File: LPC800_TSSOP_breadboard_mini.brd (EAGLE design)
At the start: 31.1 x 15.9 mm, 16 parts, among them Q1 12MHz

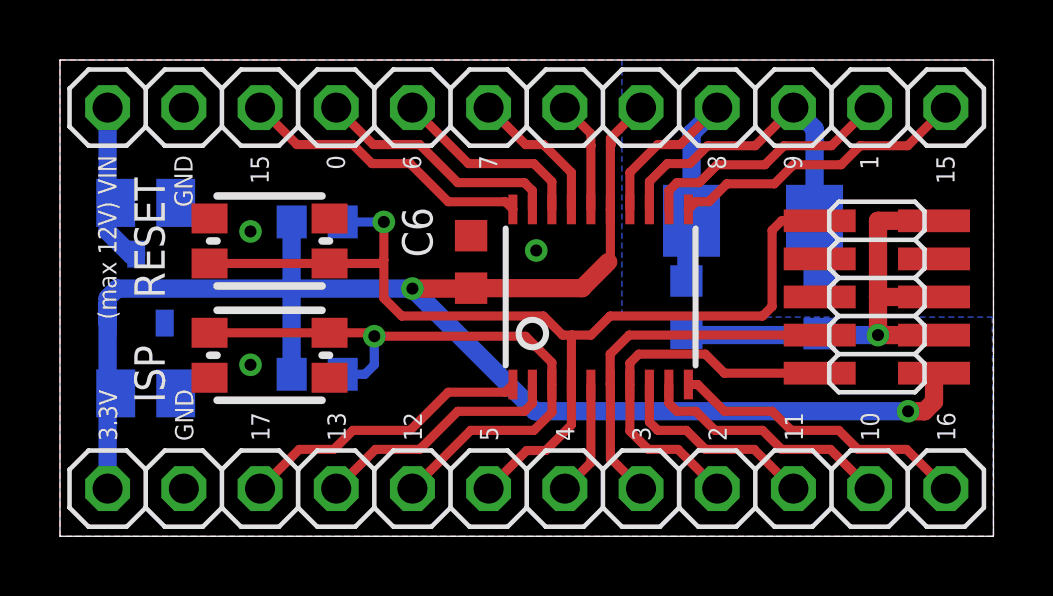
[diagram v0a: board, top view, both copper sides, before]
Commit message: * finished LPC800 mini board * fixed pin 1 for JTAG connection - TODO: Printout inspection and checks for the button layout
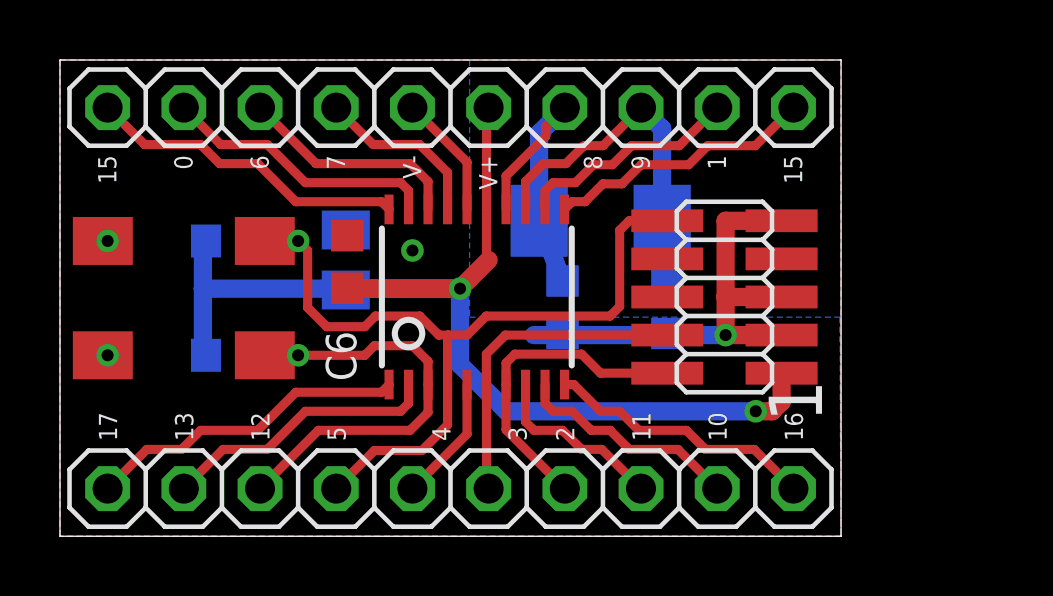
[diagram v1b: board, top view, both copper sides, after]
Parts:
- removed C5: 1u, bart_rcl:C0805K
- removed JP4, JP5: (no value), SquantorConnectors:1X12_NORMAL_OCT
- removed U$3: RESET, SquantorButtons:KMR2
- removed U$4: ISP, SquantorButtons:KMR2
- added JP1, JP2: (no value), SquantorConnectors:1X10_NORMAL_OCT
- added U$1: TACT_2PINDTSM3, SquantorButtons:DTSM3
- C6: value (none) -> 100n
- U$2: value TS9011 -> TACT_2PINDTSM3; device bart_ic:SOT23-3 -> SquantorButtons:DTSM3
- moved C4 8.01 mm to (9.53, 9.21), turned to 90 degrees
- moved C3 5.08 mm to (20.2, 7.63)
- moved JP3 5.08 mm to (22.1, 7.98)
- moved Q1 5.08 mm to (18.0, 10.5)
- moved C6 4.13 mm to (9.58, 9.14)
- moved LOGO2 4.13 mm to (14.5, 3.91)
- moved LPC812 4.13 mm to (13.9, 7.98)
- moved C2 4.13 mm to (16.8, 7.63)
- moved R1 2.93 mm to (5.71, 6.03)
- moved R2 2.93 mm to (5.71, 9.84)
- moved U$2 2.73 mm to (4.13, 6.03), flipped to the top, turned to 180 degrees
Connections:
- removed net VCCIO: C5.1, JP4.12, U$2.3
- net PIO0_0: now also JP2.9; no longer JP4.9
- net PIO0_1: now also JP2.2; no longer JP4.2
- net PIO0_10: now also JP1.9; no longer JP5.11
- net PIO0_11: now also JP1.8; no longer JP5.10
- net PIO0_12: now also JP1.3, U$2.P$1; no longer JP5.5, U$4.1, U$4.2
- net PIO0_13: now also JP1.2; no longer JP5.4
- net PIO0_14: now also JP2.10; no longer JP4.10
- net PIO0_15: now also JP2.1; no longer JP4.1
- net PIO0_16: now also JP1.10; no longer JP5.12
- net PIO0_17: now also JP1.1; no longer JP5.3
- net PIO0_2: now also JP1.7; no longer JP5.9
- net PIO0_3: now also JP1.6; no longer JP5.8
- net PIO0_4: now also JP1.5; no longer JP5.7
- net PIO0_5: now also JP1.4, U$1.P$1; no longer JP5.6, U$3.1, U$3.2
- net PIO0_6: now also JP2.8; no longer JP4.8
- net PIO0_7: now also JP2.7; no longer JP4.7
- net PIO0_8: now also JP2.4; no longer JP4.4
- net PIO0_9: now also JP2.3; no longer JP4.3
- net VDD: now also JP2.5; no longer JP4.5, JP5.1, U$2.2
- net VSS: now also JP2.6, U$1.P$2, U$2.P$2; no longer C5.2, JP4.11, JP4.6, JP5.2, U$2.1, U$3.3, U$3.4, U$4.3, U$4.4
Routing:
- net VDD: track 56.1 -> 38.4 mm
- net PIO0_5: track 34.9 -> 28.2 mm
- net PIO0_12: track 21.3 -> 15.5 mm
- net VCCIO: track 5.68 -> 0.00 mm
- net PIO0_2: track 12.7 -> 10.8 mm
- net PIO0_3: track 12.2 -> 10.8 mm
- net PIO0_1: track 8.46 -> 7.51 mm
- net PIO0_10: track 8.50 -> 7.54 mm
- net PIO0_7: track 4.89 -> 5.84 mm
- net PIO0_6: track 6.60 -> 7.55 mm
- net PIO0_17: track 9.87 -> 10.8 mm
- net PIO0_14: track 9.84 -> 10.8 mm
- net PIO0_13: track 8.34 -> 9.30 mm
- net PIO0_0: track 8.31 -> 9.26 mm
- net PIO0_15: track 9.99 -> 9.04 mm
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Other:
- board size 31.1 x 15.9 mm -> 26 x 15.9 mm
- board text added: "V+"
- board text added: "V-"
- board text removed: "(max 12V) VIN"
- board text removed: "3.3V"
- board text removed: "GND"

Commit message: * updated boards with cheaper buttons, better layout and indexed JTAG header
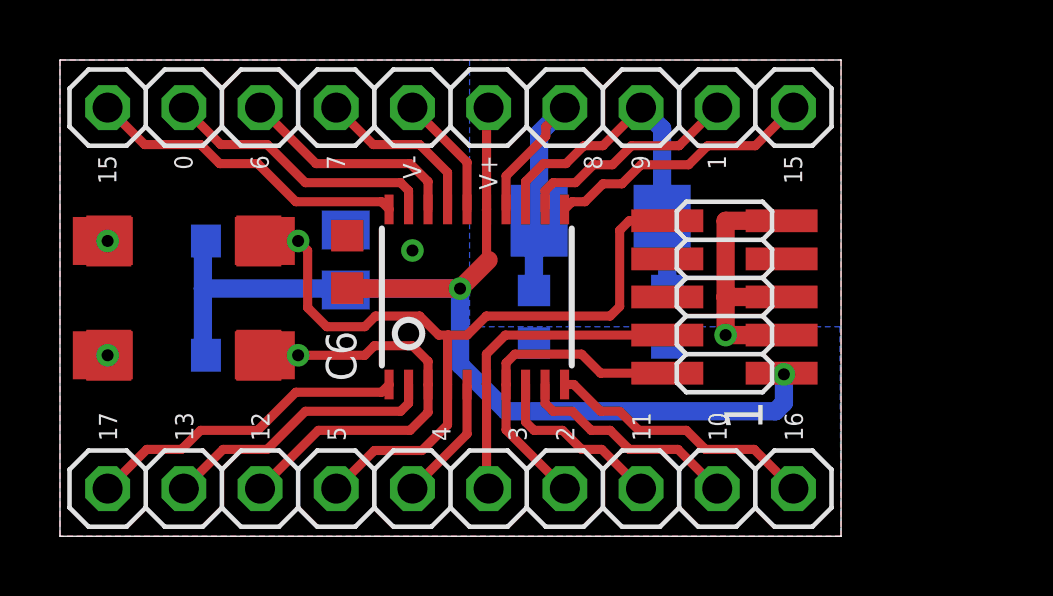
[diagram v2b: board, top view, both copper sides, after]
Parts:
- added U$3, U$4: TACT_2PIN, SquantorButtons:TD-85XU
- JP3: device bart_connectors:2X05_1.27_SMD -> SquantorConnectors:2X05_1.27_SMD
- moved C2 1.00 mm to (15.8, 7.32)
- moved C3 0.32 mm to (20.2, 7.32)
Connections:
- net PIO0_12: now also U$4.P$1
- net PIO0_5: now also U$3.P$1
- net VSS: now also U$3.P$2, U$4.P$2
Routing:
- net VSS: track 19.9 -> 13.6 mm
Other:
- board text added: "V2014.10.08"
- board text removed: "V2014.05.29"
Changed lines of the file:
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@@
 <?xml version="1.0" encoding="utf-8"?>
 <!DOCTYPE eagle SYSTEM "eagle.dtd">
-<eagle version="7.1.0">
+<eagle version="6.5.0">
 <drawing>
 <settings>
@@
 <layers>
 <layer number="1" name="Top" color="4" fill="1" visible="yes" active="yes"/>
-<layer number="16" name="Bottom" color="1" fill="1" visible="no" active="yes"/>
+<layer number="16" name="Bottom" color="1" fill="1" visible="yes" active="yes"/>
 <layer number="17" name="Pads" color="2" fill="1" visible="yes" active="yes"/>
 <layer number="18" name="Vias" color="2" fill="1" visible="yes" active="yes"/>
-<layer number="19" name="Unrouted" color="6" fill="1" visible="no" active="yes"/>
+<layer number="19" name="Unrouted" color="6" fill="1" visible="yes" active="yes"/>
 <layer number="20" name="Dimension" color="15" fill="1" visible="yes" active="yes"/>
 <layer number="21" name="tPlace" color="7" fill="1" visible="yes" active="yes"/>
-<layer number="22" name="bPlace" color="7" fill="1" visible="no" active="yes"/>
+<layer number="22" name="bPlace" color="7" fill="1" visible="yes" active="yes"/>
 <layer number="23" name="tOrigins" color="15" fill="1" visible="yes" active="yes"/>
-<layer number="24" name="bOrigins" color="15" fill="1" visible="no" active="yes"/>
+<layer number="24" name="bOrigins" color="15" fill="1" visible="yes" active="yes"/>
 <layer number="25" name="tNames" color="7" fill="1" visible="yes" active="yes"/>
-<layer number="26" name="bNames" color="7" fill="1" visible="no" active="yes"/>
+<layer number="26" name="bNames" color="7" fill="1" visible="yes" active="yes"/>
 <layer number="27" name="tValues" color="7" fill="1" visible="yes" active="yes"/>
-<layer number="28" name="bValues" color="7" fill="1" visible="no" active="yes"/>
+<layer number="28" name="bValues" color="7" fill="1" visible="yes" active="yes"/>
 <layer number="29" name="tStop" color="7" fill="3" visible="no" active="yes"/>
 <layer number="30" name="bStop" color="7" fill="6" visible="no" active="yes"/>
@@
 <wire x1="0" y1="15.875" x2="0" y2="0" width="0" layer="20"/>
 <wire x1="0" y1="0" x2="26.035" y2="0" width="0" layer="20"/>
-<text x="24.13" y="3.4925" size="1.016" layer="22" rot="MR90">V2014.05.29</text>
+<text x="24.13" y="3.4925" size="1.016" layer="22" rot="MR90">V2014.10.08</text>
 <text x="1.905" y="3.175" size="0.6096" layer="25" rot="R90">17</text>
 <text x="4.445" y="3.175" size="0.6096" layer="25" rot="R90">13</text>
@@
 <text x="11.43" y="12.7" size="0.6096" layer="25" rot="R270">V-</text>
 <text x="13.97" y="12.7" size="0.6096" layer="25" rot="R270">V+</text>
-<text x="25.4" y="3.81" size="1.778" layer="25" rot="R90">1</text>
 </plain>
 <attributes>
@@
 <pass name="Default">
 <param name="RoutingGrid" value="50mil"/>
-<param name="AutoGrid" value="1"/>
-<param name="Efforts" value="0"/>
-<param name="TopRouterVariant" value="1"/>
 <param name="tpViaShape" value="round"/>
 <param name="PrefDir.1" value="|"/>
@@
 <attribute name="VALUE" x="22.5425" y="8.255" size="1.016" layer="28" rot="MR90"/>
 </element>
-<element name="C2" library="SquantorRCL" package="C0603K" value="22p" x="16.7513" y="7.6327" smashed="yes" rot="MR270">
-<attribute name="NAME" x="14.6939" y="6.858" size="1.016" layer="26" rot="MR90"/>
-</element>
-<element name="C3" library="SquantorRCL" package="C0603K" value="22p" x="20.2438" y="7.6327" smashed="yes" rot="MR270">
-<attribute name="NAME" x="18.1864" y="6.858" size="1.016" layer="26" rot="MR90"/>
+<element name="C2" library="SquantorRCL" package="C0603K" value="22p" x="15.7988" y="7.3152" smashed="yes" rot="MR270">
+<attribute name="NAME" x="13.7414" y="6.5405" size="1.016" layer="26" rot="MR90"/>
+</element>
+<element name="C3" library="SquantorRCL" package="C0603K" value="22p" x="20.2438" y="7.3152" smashed="yes" rot="MR270">
+<attribute name="NAME" x="18.1864" y="6.5405" size="1.016" layer="26" rot="MR90"/>
 </element>
 <element name="LPC812" library="LPC800" package="TSSOP20" value="LPC812M101JDH20" x="13.8938" y="7.9756" smashed="yes"/>
-<element name="JP3" library="bart_connectors" package="2X05_1.27_SMD" value="JTAG" x="22.1488" y="7.9756" smashed="yes" rot="R90">
+<element name="JP3" library="SquantorConnectors" package="2X05_1.27_SMD" value="JTAG" x="22.1488" y="7.9756" smashed="yes" rot="R90">
 <attribute name="VALUE" x="18.6182" y="6.7437" size="1.016" layer="27" rot="R90"/>
 </element>
@@
 <element name="U$1" library="SquantorButtons" package="DTSM3" value="TACT_2PINDTSM3" x="4.1275" y="9.8425" smashed="yes" rot="R180"/>
 <element name="U$2" library="SquantorButtons" package="DTSM3" value="TACT_2PINDTSM3" x="4.1275" y="6.0325" smashed="yes" rot="R180"/>
+<element name="U$3" library="SquantorButtons" package="TD-85XU" value="TACT_2PIN" x="4.1275" y="9.8425" smashed="yes" rot="R180"/>
+<element name="U$4" library="SquantorButtons" package="TD-85XU" value="TACT_2PIN" x="4.1275" y="6.0325" smashed="yes" rot="R180"/>
 </elements>
 <signals>
@@
 <wire x1="15.5188" y1="11.8231" x2="16.1163" y2="12.4206" width="0.3048" layer="1"/>
 <wire x1="16.1163" y1="12.4206" x2="16.8656" y2="12.4206" width="0.3048" layer="1"/>
-<wire x1="20.2438" y1="8.5077" x2="20.2438" y2="10.9781" width="0.6096" layer="16"/>
+<wire x1="20.2438" y1="8.1902" x2="20.2438" y2="10.9781" width="0.6096" layer="16"/>
 <wire x1="20.2438" y1="10.9781" x2="20.0713" y2="10.5156" width="0.6096" layer="16"/>
 <wire x1="16.8656" y1="12.4206" x2="17.4625" y2="13.0175" width="0.3048" layer="1"/>
@@
 <contactref element="Q1" pad="1"/>
 <contactref element="C2" pad="1"/>
-<wire x1="16.7513" y1="8.5077" x2="15.7988" y2="10.9781" width="0.6096" layer="16"/>
+<wire x1="15.7988" y1="8.1902" x2="15.7988" y2="10.9781" width="0.6096" layer="16"/>
 <wire x1="15.7988" y1="10.9781" x2="15.9713" y2="10.5156" width="0.6096" layer="16"/>
 <wire x1="15.9713" y1="10.5156" x2="15.9713" y2="13.4313" width="0.6096" layer="16"/>
@@
 <via x="22.1869" y="6.7056" extent="1-16" drill="0.4" shape="octagon"/>
 <wire x1="22.1869" y1="6.7056" x2="24.0538" y2="6.7056" width="0.6096" layer="1"/>
-<wire x1="22.1869" y1="6.7056" x2="15.7988" y2="6.7056" width="0.6096" layer="16"/>
 <polygon width="0.254" layer="1" isolate="0.3048">
 <vertex x="0" y="15.875"/>
@@
 <vertex x="0" y="15.875"/>
 <vertex x="13.6525" y="15.875"/>
-<vertex x="13.6525" y="7.3025"/>
-<vertex x="25.9969" y="7.3025"/>
+<vertex x="13.6525" y="6.985"/>
+<vertex x="25.9969" y="6.985"/>
 <vertex x="26.035" y="0"/>
 <vertex x="0" y="0"/>
@@
 <wire x1="13.5688" y1="10.8934" x2="13.5688" y2="12.4662" width="0.3048" layer="1"/>
 <wire x1="13.5688" y1="12.4662" x2="11.7475" y2="14.2875" width="0.3048" layer="1"/>
+<contactref element="U$4" pad="P$2"/>
+<contactref element="U$3" pad="P$2"/>
 </signal>
 <signal name="VDD">
@@
 <contactref element="R2" pad="1"/>
 <wire x1="14.2113" y1="10.8859" x2="14.2188" y2="10.8934" width="0.3048" layer="1"/>
-<wire x1="24.0538" y1="5.4356" x2="24.0538" y2="4.4831" width="0.6096" layer="1"/>
-<via x="23.1902" y="4.1656" extent="1-16" drill="0.4" shape="octagon"/>
 <contactref element="C6" pad="1"/>
-<wire x1="24.0538" y1="4.4831" x2="23.7363" y2="4.1656" width="0.6096" layer="1"/>
-<wire x1="23.7363" y1="4.1656" x2="23.1902" y2="4.1656" width="0.6096" layer="1"/>
 <contactref element="JP2" pad="5"/>
 <contactref element="JP2" pad="5"/>
-<wire x1="23.1902" y1="4.1656" x2="14.8844" y2="4.1656" width="0.6096" layer="16"/>
+<wire x1="23.8506" y1="4.1656" x2="14.8844" y2="4.1656" width="0.6096" layer="16"/>
 <wire x1="14.8844" y1="4.1656" x2="13.335" y2="5.715" width="0.6096" layer="16"/>
 <wire x1="13.335" y1="5.715" x2="13.335" y2="8.255" width="0.6096" layer="16"/>
@@
 <wire x1="10.146" y1="8.269" x2="10.16" y2="8.255" width="0.6096" layer="1"/>
 <wire x1="10.16" y1="8.255" x2="13.335" y2="8.255" width="0.6096" layer="1"/>
+<wire x1="23.8506" y1="4.1656" x2="24.13" y2="4.445" width="0.6096" layer="16"/>
+<wire x1="24.13" y1="4.445" x2="24.13" y2="5.3975" width="0.6096" layer="16"/>
+<via x="24.13" y="5.3975" extent="1-16" drill="0.4" shape="octagon"/>
+<wire x1="24.13" y1="5.3975" x2="24.0919" y2="5.3975" width="0.6096" layer="1"/>
+<wire x1="24.0919" y1="5.3975" x2="24.0538" y2="5.4356" width="0.6096" layer="1"/>
 </signal>
 <signal name="PIO0_0">
@@
 <wire x1="7.9375" y1="9.8425" x2="8.255" y2="9.525" width="0.3048" layer="1"/>
 <wire x1="6.8275" y1="9.8425" x2="7.9375" y2="9.8425" width="0.3048" layer="1"/>
+<contactref element="U$3" pad="P$1"/>
+<wire x1="6.6275" y1="9.8425" x2="6.8275" y2="9.8425" width="0.4064" layer="1"/>
 </signal>
 <signal name="PIO0_6">
@@
 <wire x1="6.565" y1="6.0325" x2="7.9375" y2="6.0325" width="0.3048" layer="16"/>
 <via x="7.9375" y="6.0325" extent="1-16" drill="0.4" shape="octagon"/>
+<contactref element="U$4" pad="P$1"/>
+<wire x1="6.6275" y1="6.0325" x2="6.8275" y2="6.0325" width="0.4064" layer="1"/>
 </signal>
 <signal name="PIO0_11">

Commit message: * small changes preparing for commit to OSH park
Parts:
- moved C2 0.32 mm to (15.8, 7.00)
- moved C3 0.32 mm to (20.2, 7.00)
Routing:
- net VSS: track 13.6 -> 8.56 mm
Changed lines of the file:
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@@
 <?xml version="1.0" encoding="utf-8"?>
 <!DOCTYPE eagle SYSTEM "eagle.dtd">
-<eagle version="6.5.0">
+<eagle version="7.1.0">
 <drawing>
 <settings>
@@
 <layer number="20" name="Dimension" color="15" fill="1" visible="yes" active="yes"/>
 <layer number="21" name="tPlace" color="7" fill="1" visible="yes" active="yes"/>
-<layer number="22" name="bPlace" color="7" fill="1" visible="yes" active="yes"/>
+<layer number="22" name="bPlace" color="7" fill="1" visible="no" active="yes"/>
 <layer number="23" name="tOrigins" color="15" fill="1" visible="yes" active="yes"/>
-<layer number="24" name="bOrigins" color="15" fill="1" visible="yes" active="yes"/>
+<layer number="24" name="bOrigins" color="15" fill="1" visible="no" active="yes"/>
 <layer number="25" name="tNames" color="7" fill="1" visible="yes" active="yes"/>
-<layer number="26" name="bNames" color="7" fill="1" visible="yes" active="yes"/>
+<layer number="26" name="bNames" color="7" fill="1" visible="no" active="yes"/>
 <layer number="27" name="tValues" color="7" fill="1" visible="yes" active="yes"/>
-<layer number="28" name="bValues" color="7" fill="1" visible="yes" active="yes"/>
+<layer number="28" name="bValues" color="7" fill="1" visible="no" active="yes"/>
 <layer number="29" name="tStop" color="7" fill="3" visible="no" active="yes"/>
 <layer number="30" name="bStop" color="7" fill="6" visible="no" active="yes"/>
@@
 <wire x1="0" y1="15.875" x2="0" y2="0" width="0" layer="20"/>
 <wire x1="0" y1="0" x2="26.035" y2="0" width="0" layer="20"/>
-<text x="24.13" y="3.4925" size="1.016" layer="22" rot="MR90">V2014.10.08</text>
+<text x="23.1775" y="3.4925" size="1.016" layer="22" rot="MR0">V2014.10.08</text>
 <text x="1.905" y="3.175" size="0.6096" layer="25" rot="R90">17</text>
 <text x="4.445" y="3.175" size="0.6096" layer="25" rot="R90">13</text>
@@
 <pass name="Default">
 <param name="RoutingGrid" value="50mil"/>
+<param name="AutoGrid" value="1"/>
+<param name="Efforts" value="0"/>
+<param name="TopRouterVariant" value="1"/>
 <param name="tpViaShape" value="round"/>
 <param name="PrefDir.1" value="|"/>
@@
 <elements>
 <element name="Q1" library="bart_crystals" package="CRYSTAL_5.0X3.2" value="12MHz" x="18.0213" y="10.5156" smashed="yes" rot="MR180">
-<attribute name="NAME" x="13.6525" y="9.8425" size="1.016" layer="26" rot="MR90"/>
-<attribute name="VALUE" x="22.5425" y="8.255" size="1.016" layer="28" rot="MR90"/>
-</element>
-<element name="C2" library="SquantorRCL" package="C0603K" value="22p" x="15.7988" y="7.3152" smashed="yes" rot="MR270">
-<attribute name="NAME" x="13.7414" y="6.5405" size="1.016" layer="26" rot="MR90"/>
-</element>
-<element name="C3" library="SquantorRCL" package="C0603K" value="22p" x="20.2438" y="7.3152" smashed="yes" rot="MR270">
-<attribute name="NAME" x="18.1864" y="6.5405" size="1.016" layer="26" rot="MR90"/>
+<attribute name="NAME" x="21.59" y="9.8425" size="1.016" layer="26" rot="MR90"/>
+<attribute name="VALUE" x="22.86" y="8.255" size="1.016" layer="28" rot="MR90"/>
+</element>
+<element name="C2" library="SquantorRCL" package="C0603K" value="22p" x="15.7988" y="6.9977" smashed="yes" rot="MR270">
+<attribute name="NAME" x="16.9164" y="6.223" size="1.016" layer="26" rot="MR90"/>
+</element>
+<element name="C3" library="SquantorRCL" package="C0603K" value="22p" x="20.2438" y="6.9977" smashed="yes" rot="MR270">
+<attribute name="NAME" x="18.1864" y="6.223" size="1.016" layer="26" rot="MR90"/>
 </element>
 <element name="LPC812" library="LPC800" package="TSSOP20" value="LPC812M101JDH20" x="13.8938" y="7.9756" smashed="yes"/>
@@
 </element>
 <element name="C4" library="bart_rcl" package="C0805K" value="1u" x="9.525" y="9.2075" smashed="yes" rot="MR90">
-<attribute name="NAME" x="10.795" y="10.4267" size="1.016" layer="26" rot="MR90"/>
+<attribute name="NAME" x="11.1125" y="10.4267" size="1.016" layer="26" rot="MR90"/>
 </element>
 <element name="R1" library="bart_rcl" package="R0603" value="10k" x="5.715" y="6.0325" smashed="yes" rot="MR180">
-<attribute name="NAME" x="5.3848" y="3.3909" size="1.016" layer="26" rot="MR90"/>
+<attribute name="NAME" x="6.7691" y="3.7973" size="1.016" layer="26" rot="MR0"/>
 </element>
 <element name="R2" library="bart_rcl" package="R0603" value="10k" x="5.715" y="9.8425" smashed="yes" rot="MR180">
-<attribute name="NAME" x="5.4991" y="10.9728" size="1.016" layer="26" rot="MR90"/>
+<attribute name="NAME" x="6.8072" y="11.2141" size="1.016" layer="26" rot="MR0"/>
 </element>
 <element name="C6" library="SquantorRCL" package="C0603K" value="100n" x="9.5758" y="9.144" smashed="yes" rot="R90">
@@
 <wire x1="15.5188" y1="11.8231" x2="16.1163" y2="12.4206" width="0.3048" layer="1"/>
 <wire x1="16.1163" y1="12.4206" x2="16.8656" y2="12.4206" width="0.3048" layer="1"/>
-<wire x1="20.2438" y1="8.1902" x2="20.2438" y2="10.9781" width="0.6096" layer="16"/>
+<wire x1="20.2438" y1="7.8727" x2="20.2438" y2="10.9781" width="0.6096" layer="16"/>
 <wire x1="20.2438" y1="10.9781" x2="20.0713" y2="10.5156" width="0.6096" layer="16"/>
 <wire x1="16.8656" y1="12.4206" x2="17.4625" y2="13.0175" width="0.3048" layer="1"/>
@@
 <contactref element="Q1" pad="1"/>
 <contactref element="C2" pad="1"/>
-<wire x1="15.7988" y1="8.1902" x2="15.7988" y2="10.9781" width="0.6096" layer="16"/>
+<wire x1="15.7988" y1="7.8727" x2="15.7988" y2="10.9781" width="0.6096" layer="16"/>
 <wire x1="15.7988" y1="10.9781" x2="15.9713" y2="10.5156" width="0.6096" layer="16"/>
 <wire x1="15.9713" y1="10.5156" x2="15.9713" y2="13.4313" width="0.6096" layer="16"/>
@@
 <contactref element="C3" pad="2"/>
 <contactref element="C4" pad="2"/>
-<via x="22.1869" y="6.7056" extent="1-16" drill="0.4" shape="octagon"/>
-<wire x1="22.1869" y1="6.7056" x2="24.0538" y2="6.7056" width="0.6096" layer="1"/>
+<via x="22.1869" y="5.4356" extent="1-16" drill="0.4" shape="octagon"/>
 <polygon width="0.254" layer="1" isolate="0.3048">
 <vertex x="0" y="15.875"/>
@@
 <vertex x="0" y="15.875"/>
 <vertex x="13.6525" y="15.875"/>
-<vertex x="13.6525" y="6.985"/>
-<vertex x="25.9969" y="6.985"/>
+<vertex x="13.6525" y="6.35"/>
+<vertex x="25.9969" y="6.35"/>
 <vertex x="26.035" y="0"/>
 <vertex x="0" y="0"/>
@@
 <wire x1="24.0538" y1="10.5156" x2="22.1869" y2="10.5156" width="0.6096" layer="1"/>
 <wire x1="22.1869" y1="10.5156" x2="22.1869" y2="7.9756" width="0.6096" layer="1"/>
-<wire x1="22.1869" y1="7.9756" x2="22.1869" y2="6.7056" width="0.6096" layer="1"/>
-<wire x1="24.0538" y1="7.9756" x2="22.1869" y2="7.9756" width="0.6096" layer="1"/>
 <contactref element="JP2" pad="6"/>
 <contactref element="JP2" pad="6"/>
